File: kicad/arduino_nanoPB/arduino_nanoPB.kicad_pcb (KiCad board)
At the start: 2 copper layers, 18.3 x 46.2 mm, 45 parts, among them J1 USB_B_Micro, P1 Digital, P2 Analog, P3 CONN_01X01, P4 CONN_01X01, P5 CONN_01X01, P6 CONN_01X01, P7 CONN_6, SW1 SW_PUSH, U1 ATMEGA328PB-AU, U2 CP2102N-A01-GQFN28, U3 AP1117-50, U4 AP1117-50, Y1 Resonator

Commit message: updates
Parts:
- D1: value Green RED -> Green
- D2: value Red LED -> Red
- D3, D4: value Yellow LED -> Yellow
- L1: value L -> ferite bead
- R1, R2: value 22 -> 20
- U2: value CP2102N-A01-GQFN28 -> CP2102
- U4: value AP1117-50 -> AP1117-33
- Y1: value Resonator -> 16MHz
- moved L1 0.89 mm to (152.3, 109.4), turned to 270 degrees
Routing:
- net GNDPWR: track 29.2 -> 29.9 mm

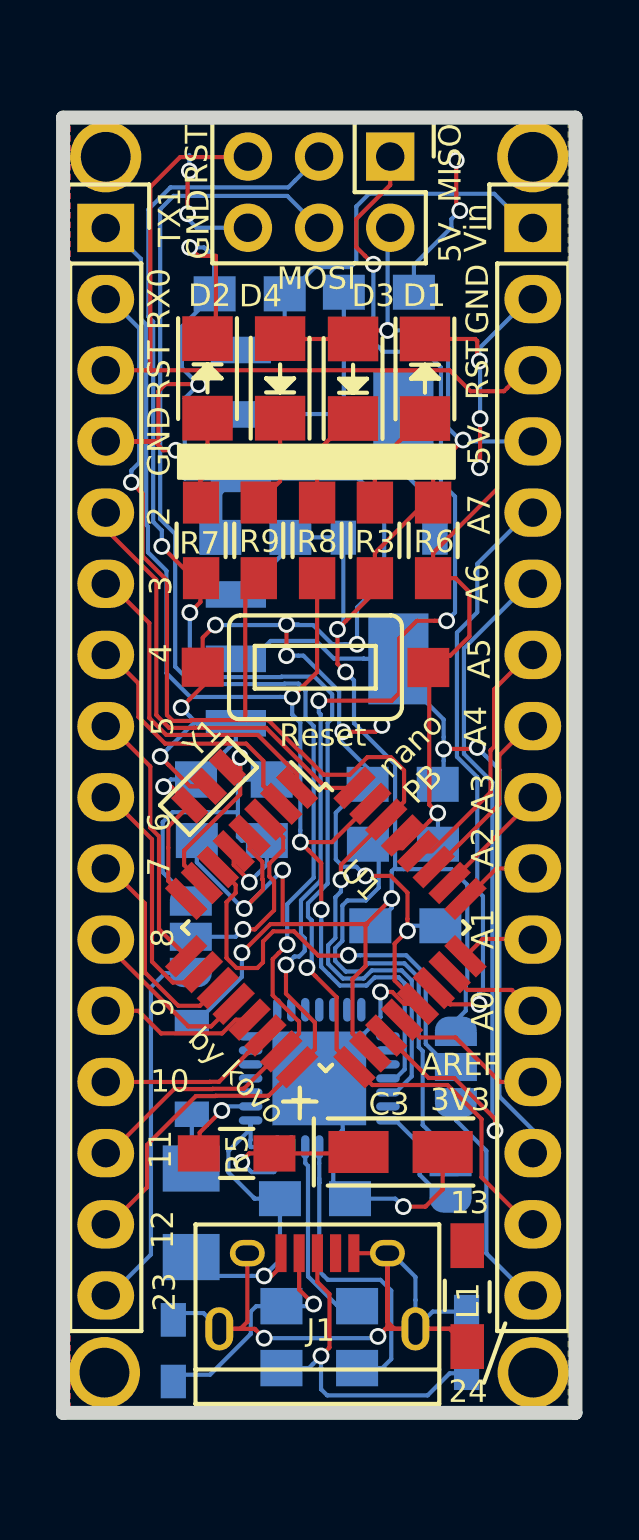
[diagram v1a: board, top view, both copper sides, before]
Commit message: pins 20,21 break out
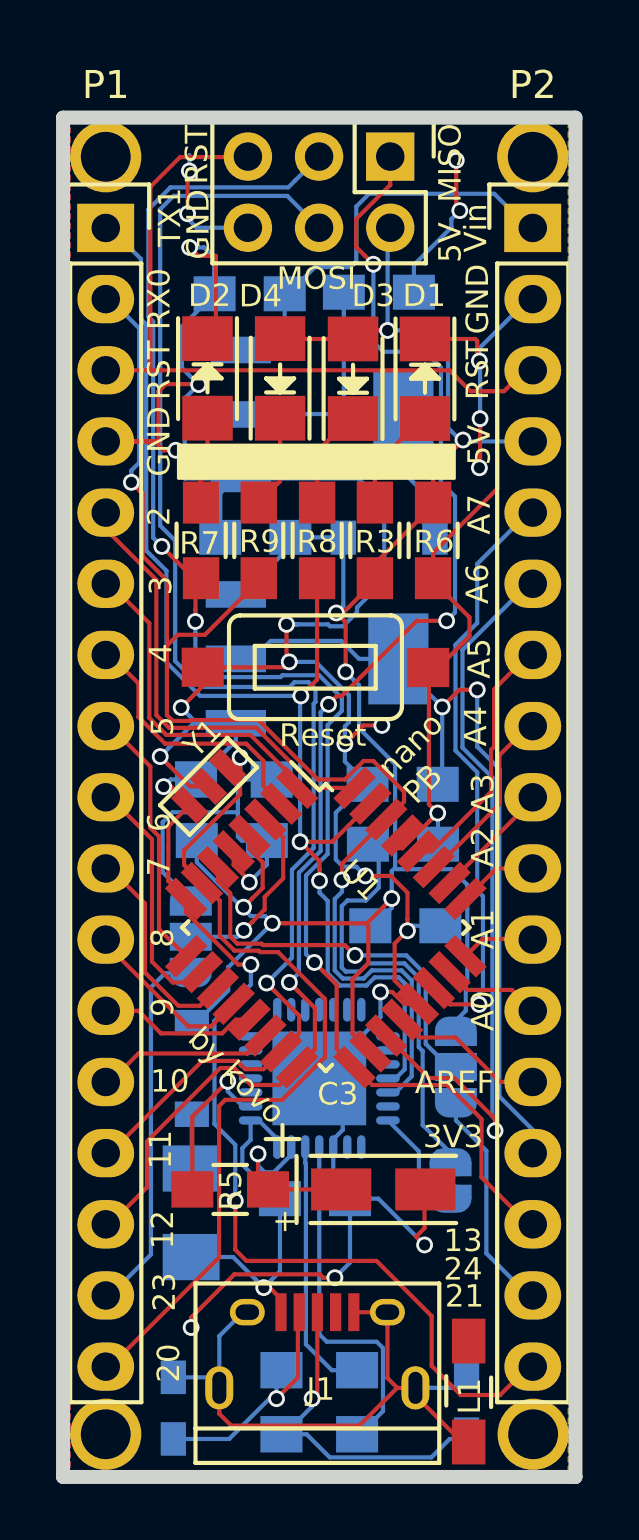
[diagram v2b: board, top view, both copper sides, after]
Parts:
- D1: value Green -> Green RED
- D2: value Red -> Red LED
- D3, D4: value Yellow -> Yellow LED
- L1: value ferite bead -> L
- P1, P2: footprint Pin_Headers.pretty:Pin_Header_Straight_1x16 -> Pin_Headers.pretty:Pin_Header_Straight_1x17
- U2: value CP2102 -> CP2102N-A01-GQFN28
- Y1: value 16MHz -> Resonator
- moved L1 3.41 mm to (152.4, 112.8)
- moved R2 2.36 mm to (147.1, 114.3)
- moved R1 2.29 mm to (147.1, 112.0)
- moved P4 2.20 mm to (139.4, 114.3)
- moved P5 2.20 mm to (154.7, 114.3)
- moved TH2 2.18 mm to (152.3, 113.2)
- moved J1 2.11 mm to (147.0, 111.5)
- moved TH1 2.05 mm to (141.9, 113.4)
- moved C3 1.47 mm to (149.4, 105.6)
- moved R5 1.31 mm to (143.9, 105.6)
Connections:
- R4 pad 1: /XTAL1 -> /20
- R4 pad 2: /XTAL2 -> /21
- U1 pad 7: /XTAL1 -> /20
- U1 pad 8: /XTAL2 -> /21
- Y1 pad 1: /XTAL2 -> /21
- Y1 pad 3: /XTAL1 -> /20
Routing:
- net /21: track 0.00 -> 35.2 mm, vias 0 -> 3
- net /20: track 0.00 -> 32.4 mm, vias 0 -> 1
- net /XTAL1: track 7.96 -> 0.00 mm, vias 1 -> 0
- net GNDPWR: track 29.9 -> 22.5 mm, vias 2 -> 0
- net GND: track 129.6 -> 136.9 mm
- net /XTAL2: track 6.39 -> 0.00 mm, vias 1 -> 0
- net +5V: track 78.0 -> 74.7 mm, vias 8 -> 7
- net /#RST: track 2.96 -> 5.78 mm
- net /DD-: track 6.85 -> 9.26 mm
- net /MEGA6: track 16.4 -> 14.1 mm
- net 3V3: track 30.3 -> 32.1 mm
- net /DD+: track 11.3 -> 12.8 mm
- net /0(Rx): track 47.2 -> 45.6 mm
- net /12(MISO): track 51.0 -> 49.8 mm
- net /Reset: track 47.8 -> 46.9 mm
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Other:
- board size 18.3 x 46.2 mm -> 18.3 x 48.5 mm
- board text added: "20"
- board text added: "21"
